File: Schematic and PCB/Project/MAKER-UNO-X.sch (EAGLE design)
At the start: 102 parts, among them CN1 USB-5PIN_(MICRO-B-RA), Q1 60V 600mA, Q10 50V 220mA, Q11 50V 220mA, Q12 50V 220mA, Q13 50V 220mA, Q14 50V 220mA, Q2 50V 220mA, Q3 50V 220mA, Q4 50V 220mA, Q5 50V 220mA, Q6 50V 220mA, Q7 50V 220mA, Q8 50V 220mA, Q9 50V 220mA, U2 CH340G_(SOIC-16N), U3 555_(SOIC-08N), U4 3.3V 500mA, Y1 16MHz

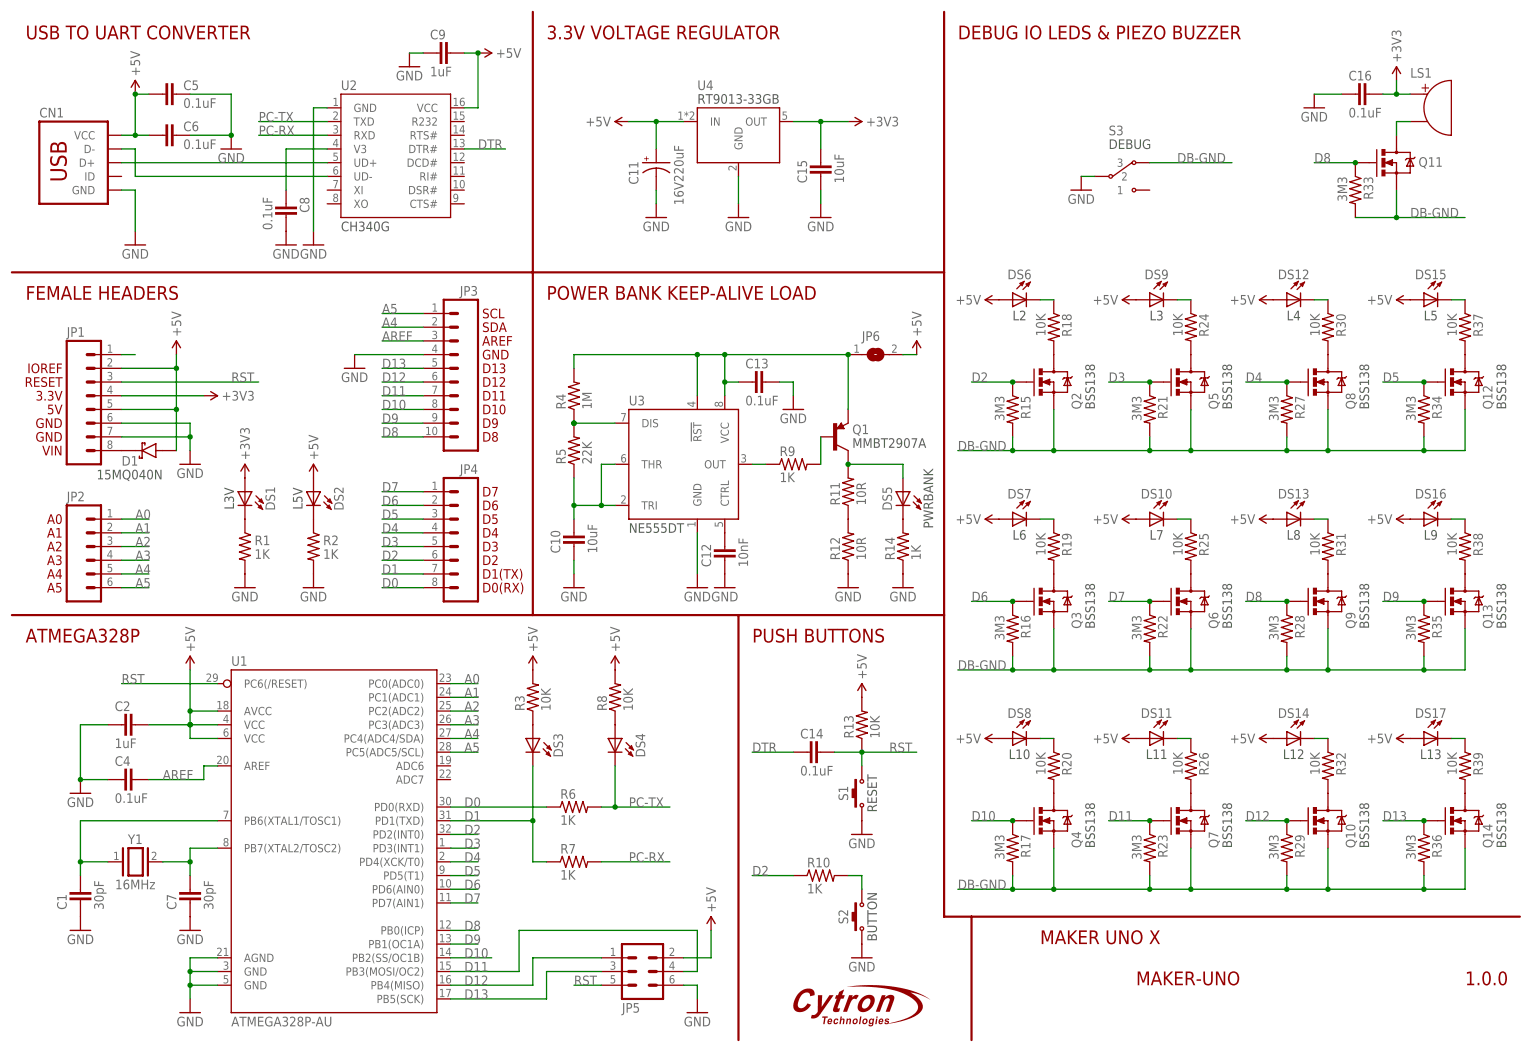
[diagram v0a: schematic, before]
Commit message: Modified the overlay.
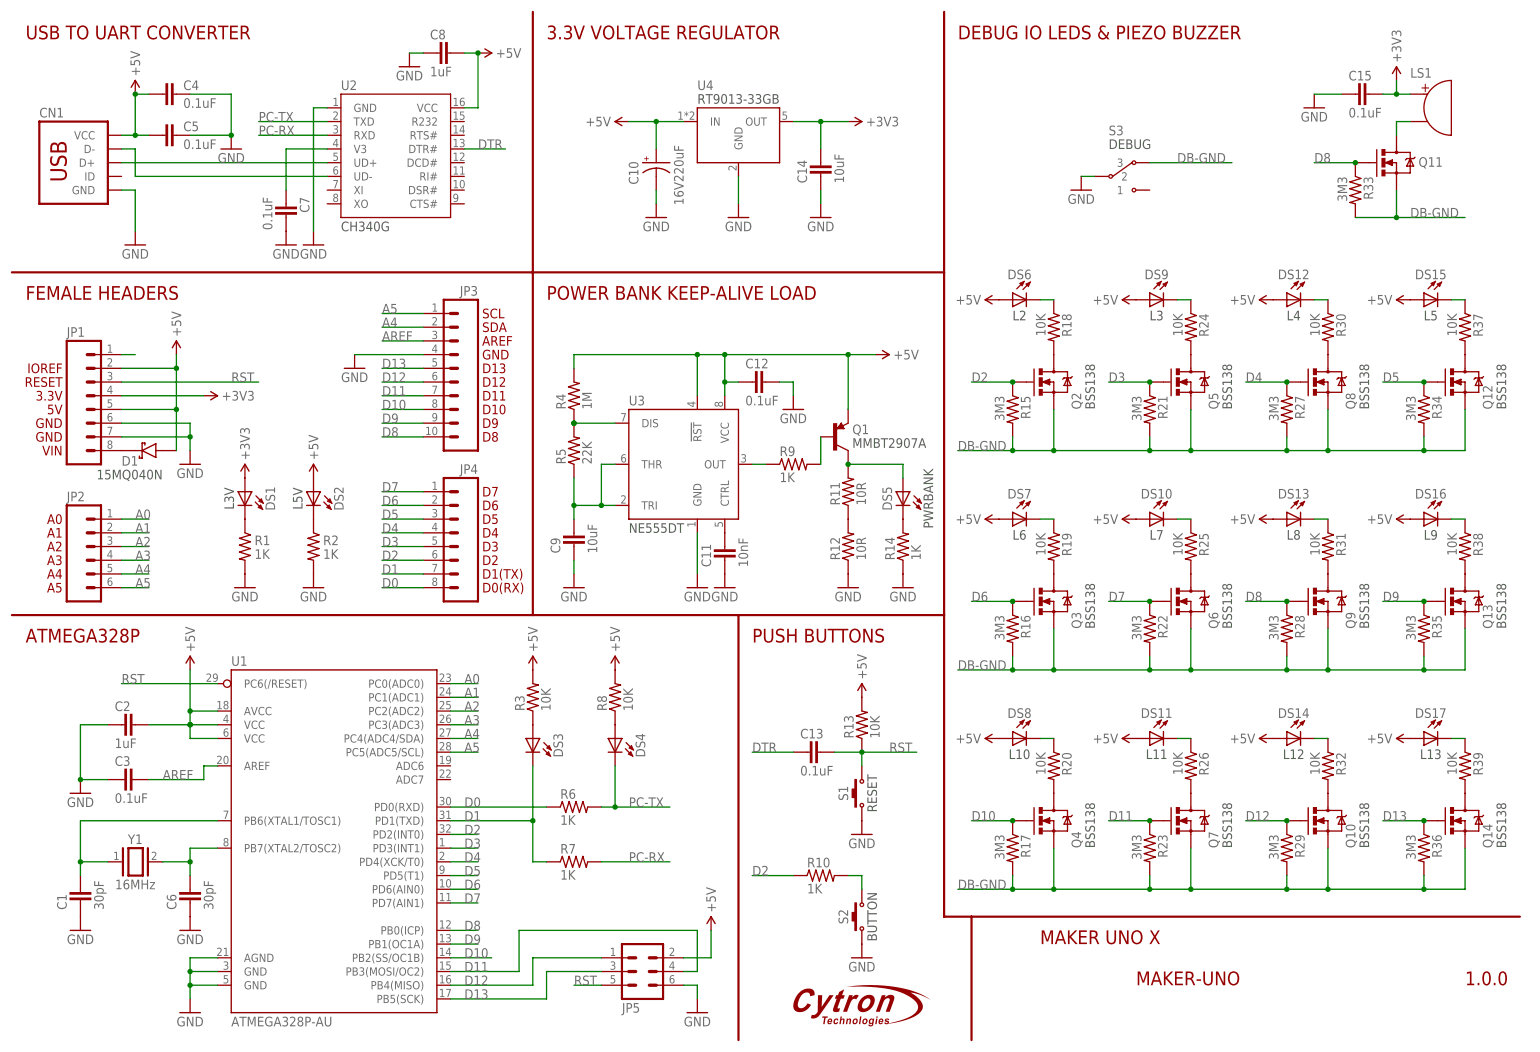
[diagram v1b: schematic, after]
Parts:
- removed C16: 0.1uF, Others:CAP-C_0.1UF_(1608)
- removed JP6: SJ-NC, Misc:SJ-NC
- added C3: 0.1uF, Others:CAP-C_0.1UF_(1608)
- C10: value 10uF -> 16V220uF; device Others:CAP-C_10UF_(2012) -> Others:CAP-E-ALUMINIUM_16V220UF_(CHEMICON-F55)
- C11: value 16V220uF -> 10nF; device Others:CAP-E-ALUMINIUM_16V220UF_(CHEMICON-F55) -> Others:CAP-C_10NF_(1608)
- C12: value 10nF -> 0.1uF; device Others:CAP-C_10NF_(1608) -> Others:CAP-C_0.1UF_(1608)
- C14: value 0.1uF -> 10uF; device Others:CAP-C_0.1UF_(1608) -> Others:CAP-C_10UF_(2012)
- C15: value 10uF -> 0.1uF; device Others:CAP-C_10UF_(2012) -> Others:CAP-C_0.1UF_(1608)
- C6: value 0.1uF -> 30pF; device Others:CAP-C_0.1UF_(1608) -> Others:CAP-C_30PF_(1608)
- C7: value 30pF -> 0.1uF; device Others:CAP-C_30PF_(1608) -> Others:CAP-C_0.1UF_(1608)
- C8: value 0.1uF -> 1uF; device Others:CAP-C_0.1UF_(1608) -> Others:CAP-C_1UF_(1608)
- C9: value 1uF -> 10uF; device Others:CAP-C_1UF_(1608) -> Others:CAP-C_10UF_(2012)
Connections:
- removed net N$17: C13.2, JP6.1, Q1.E, R4.2, U3.!RST, U3.VCC
- net +3V3: now also C14.1; no longer C16.1
- net +5V: now also C10.+, C12.2, C4.1, C8.1, Q1.E, R4.2, U3.!RST, U3.VCC; no longer C11.+, C6.1, C9.1, JP6.2
- net AREF: now also C3.1; no longer C4.1
- net DTR: now also C13.2; no longer C14.2
- net GND: now also C10.-, C11.2, C12.1, C14.2, C3.2, C7.1, C8.2; no longer C10.2, C11.-, C12.2, C13.1, C16.2, C7.2, C8.1
- net N$1: now also C11.1; no longer C12.1
- net N$13: now also C9.1; no longer C10.1
- net N$3: now also C7.2; no longer C8.2
- net N$4: now also C6.1; no longer C7.1
- net RST: now also C13.1; no longer C14.1
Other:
- moved on the sheet: C12, C13, C14, C15, C4, C5, C6, C7, C8, C9

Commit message: Added assembly diagrams.
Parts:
- DS3: value Blue -> Red; device Others:LED_BLUE_(1608) -> Others:LED_RED_(1608)
- DS4: value Blue -> Yellow; device Others:LED_BLUE_(1608) -> Others:LED_YELLOW_(1608)
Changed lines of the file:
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@@
 <grid distance="0.1" unitdist="inch" unit="inch" style="lines" multiple="1" display="no" altdistance="0.01" altunitdist="inch" altunit="inch"/>
 <layers>
-<layer number="1" name="Top" color="4" fill="1" visible="no" active="no"/>
-<layer number="2" name="Route2" color="1" fill="3" visible="no" active="no"/>
-<layer number="3" name="Route3" color="4" fill="3" visible="no" active="no"/>
-<layer number="4" name="Route4" color="1" fill="4" visible="no" active="no"/>
-<layer number="5" name="Route5" color="4" fill="4" visible="no" active="no"/>
-<layer number="6" name="Route6" color="1" fill="8" visible="no" active="no"/>
-<layer number="7" name="Route7" color="4" fill="8" visible="no" active="no"/>
-<layer number="8" name="Route8" color="1" fill="2" visible="no" active="no"/>
-<layer number="9" name="Route9" color="4" fill="2" visible="no" active="no"/>
-<layer number="10" name="Route10" color="1" fill="7" visible="no" active="no"/>
-<layer number="11" name="Route11" color="4" fill="7" visible="no" active="no"/>
-<layer number="12" name="Route12" color="1" fill="5" visible="no" active="no"/>
-<layer number="13" name="Route13" color="4" fill="5" visible="no" active="no"/>
-<layer number="14" name="Route14" color="1" fill="6" visible="no" active="no"/>
-<layer number="15" name="Route15" color="4" fill="6" visible="no" active="no"/>
-<layer number="16" name="Bottom" color="1" fill="1" visible="no" active="no"/>
-<layer number="17" name="Pads" color="2" fill="1" visible="no" active="no"/>
-<layer number="18" name="Vias" color="2" fill="1" visible="no" active="no"/>
-<layer number="19" name="Unrouted" color="6" fill="1" visible="no" active="no"/>
-<layer number="20" name="Dimension" color="15" fill="1" visible="no" active="no"/>
-<layer number="21" name="tPlace" color="7" fill="1" visible="no" active="no"/>
-<layer number="22" name="bPlace" color="7" fill="1" visible="no" active="no"/>
-<layer number="23" name="tOrigins" color="15" fill="1" visible="no" active="no"/>
-<layer number="24" name="bOrigins" color="15" fill="1" visible="no" active="no"/>
-<layer number="25" name="tNames" color="3" fill="1" visible="no" active="no"/>
-<layer number="26" name="bNames" color="3" fill="1" visible="no" active="no"/>
-<layer number="27" name="tValues" color="5" fill="1" visible="no" active="no"/>
-<layer number="28" name="bValues" color="5" fill="1" visible="no" active="no"/>
+<layer number="1" name="Top" color="4" fill="1" visible="yes" active="no"/>
+<layer number="2" name="Route2" color="1" fill="3" visible="yes" active="no"/>
+<layer number="3" name="Route3" color="4" fill="3" visible="yes" active="no"/>
+<layer number="4" name="Route4" color="1" fill="4" visible="yes" active="no"/>
+<layer number="5" name="Route5" color="4" fill="4" visible="yes" active="no"/>
+<layer number="6" name="Route6" color="1" fill="8" visible="yes" active="no"/>
+<layer number="7" name="Route7" color="4" fill="8" visible="yes" active="no"/>
+<layer number="8" name="Route8" color="1" fill="2" visible="yes" active="no"/>
+<layer number="9" name="Route9" color="4" fill="2" visible="yes" active="no"/>
+<layer number="10" name="Route10" color="1" fill="7" visible="yes" active="no"/>
+<layer number="11" name="Route11" color="4" fill="7" visible="yes" active="no"/>
+<layer number="12" name="Route12" color="1" fill="5" visible="yes" active="no"/>
+<layer number="13" name="Route13" color="4" fill="5" visible="yes" active="no"/>
+<layer number="14" name="Route14" color="1" fill="6" visible="yes" active="no"/>
+<layer number="15" name="Route15" color="4" fill="6" visible="yes" active="no"/>
+<layer number="16" name="Bottom" color="1" fill="1" visible="yes" active="no"/>
+<layer number="17" name="Pads" color="2" fill="1" visible="yes" active="no"/>
+<layer number="18" name="Vias" color="2" fill="1" visible="yes" active="no"/>
+<layer number="19" name="Unrouted" color="6" fill="1" visible="yes" active="no"/>
+<layer number="20" name="Dimension" color="15" fill="1" visible="yes" active="no"/>
+<layer number="21" name="tPlace" color="7" fill="1" visible="yes" active="no"/>
+<layer number="22" name="bPlace" color="7" fill="1" visible="yes" active="no"/>
+<layer number="23" name="tOrigins" color="15" fill="1" visible="yes" active="no"/>
+<layer number="24" name="bOrigins" color="15" fill="1" visible="yes" active="no"/>
+<layer number="25" name="tNames" color="3" fill="1" visible="yes" active="no"/>
+<layer number="26" name="bNames" color="3" fill="1" visible="yes" active="no"/>
+<layer number="27" name="tValues" color="5" fill="1" visible="yes" active="no"/>
+<layer number="28" name="bValues" color="5" fill="1" visible="yes" active="no"/>
 <layer number="29" name="tStop" color="7" fill="3" visible="no" active="no"/>
 <layer number="30" name="bStop" color="7" fill="6" visible="no" active="no"/>
@@
 <layer number="35" name="tGlue" color="7" fill="4" visible="no" active="no"/>
 <layer number="36" name="bGlue" color="7" fill="5" visible="no" active="no"/>
-<layer number="37" name="tTest" color="7" fill="1" visible="no" active="no"/>
-<layer number="38" name="bTest" color="7" fill="1" visible="no" active="no"/>
+<layer number="37" name="tTest" color="7" fill="1" visible="yes" active="no"/>
+<layer number="38" name="bTest" color="7" fill="1" visible="yes" active="no"/>
 <layer number="39" name="tKeepout" color="4" fill="11" visible="no" active="no"/>
 <layer number="40" name="bKeepout" color="1" fill="11" visible="no" active="no"/>
@@
 <layer number="44" name="Drills" color="7" fill="1" visible="no" active="no"/>
 <layer number="45" name="Holes" color="7" fill="1" visible="no" active="no"/>
-<layer number="46" name="Milling" color="3" fill="1" visible="no" active="no"/>
-<layer number="47" name="Measures" color="7" fill="1" visible="no" active="no"/>
-<layer number="48" name="Document" color="7" fill="1" visible="no" active="no"/>
-<layer number="49" name="Reference" color="7" fill="1" visible="no" active="no"/>
-<layer number="50" name="dxf" color="7" fill="1" visible="no" active="no"/>
-<layer number="51" name="tDocu" color="6" fill="1" visible="no" active="no"/>
-<layer number="52" name="bDocu" color="6" fill="1" visible="no" active="no"/>
-<layer number="53" name="tGND_GNDA" color="7" fill="9" visible="no" active="no"/>
-<layer number="54" name="bGND_GNDA" color="1" fill="9" visible="no" active="no"/>
-<layer number="56" name="wert" color="7" fill="1" visible="no" active="no"/>
-<layer number="57" name="tCAD" color="7" fill="1" visible="no" active="no"/>
-<layer number="59" name="tCarbon" color="7" fill="1" visible="no" active="no"/>
-<layer number="60" name="bCarbon" color="7" fill="1" visible="no" active="no"/>
+<layer number="46" name="Milling" color="3" fill="1" visible="yes" active="no"/>
+<layer number="47" name="Measures" color="7" fill="1" visible="yes" active="no"/>
+<layer number="48" name="Document" color="7" fill="1" visible="yes" active="no"/>
+<layer number="49" name="Reference" color="7" fill="1" visible="yes" active="no"/>
+<layer number="50" name="dxf" color="7" fill="1" visible="yes" active="no"/>
+<layer number="51" name="tDocu" color="6" fill="1" visible="yes" active="no"/>
+<layer number="52" name="bDocu" color="6" fill="1" visible="yes" active="no"/>
+<layer number="53" name="tGND_GNDA" color="7" fill="9" visible="yes" active="no"/>
+<layer number="54" name="bGND_GNDA" color="1" fill="9" visible="yes" active="no"/>
+<layer number="56" name="wert" color="7" fill="1" visible="yes" active="no"/>
+<layer number="57" name="tCAD" color="7" fill="1" visible="yes" active="no"/>
+<layer number="59" name="tCarbon" color="7" fill="1" visible="yes" active="no"/>
+<layer number="60" name="bCarbon" color="7" fill="1" visible="yes" active="no"/>
 <layer number="90" name="Modules" color="5" fill="1" visible="yes" active="yes"/>
 <layer number="91" name="Nets" color="2" fill="1" visible="yes" active="yes"/>
@@
 </part>
 <part name="JP5" library="Header and Connector" deviceset="HEADER-2X03" device="_(S-HDR-M2X03)" value="2x3 Ways"/>
-<part name="DS4" library="Others" deviceset="LED" device="_(1608)" technology="_BLUE" value="Blue"/>
-<part name="DS3" library="Others" deviceset="LED" device="_(1608)" technology="_BLUE" value="Blue"/>
+<part name="DS4" library="Others" deviceset="LED" device="_(1608)" technology="_YELLOW" value="Yellow"/>
+<part name="DS3" library="Others" deviceset="LED" device="_(1608)" technology="_RED" value="Red"/>
 <part name="DS1" library="Others" deviceset="LED" device="_(1608)" technology="_GREEN" value="Green">
 <attribute name="LABEL" value="L3V"/>
